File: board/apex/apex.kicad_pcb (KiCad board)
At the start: 2 copper layers, 1 part

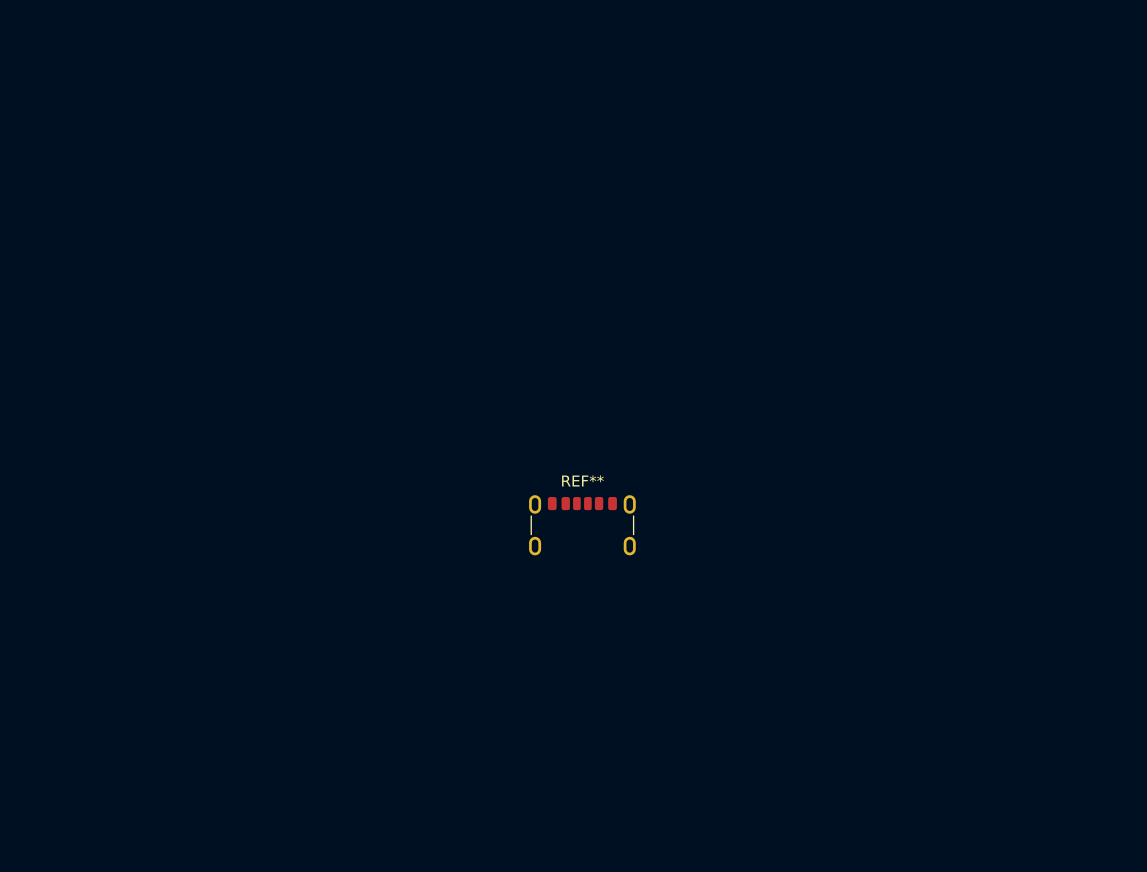
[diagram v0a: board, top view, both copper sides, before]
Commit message: added power input/outputs
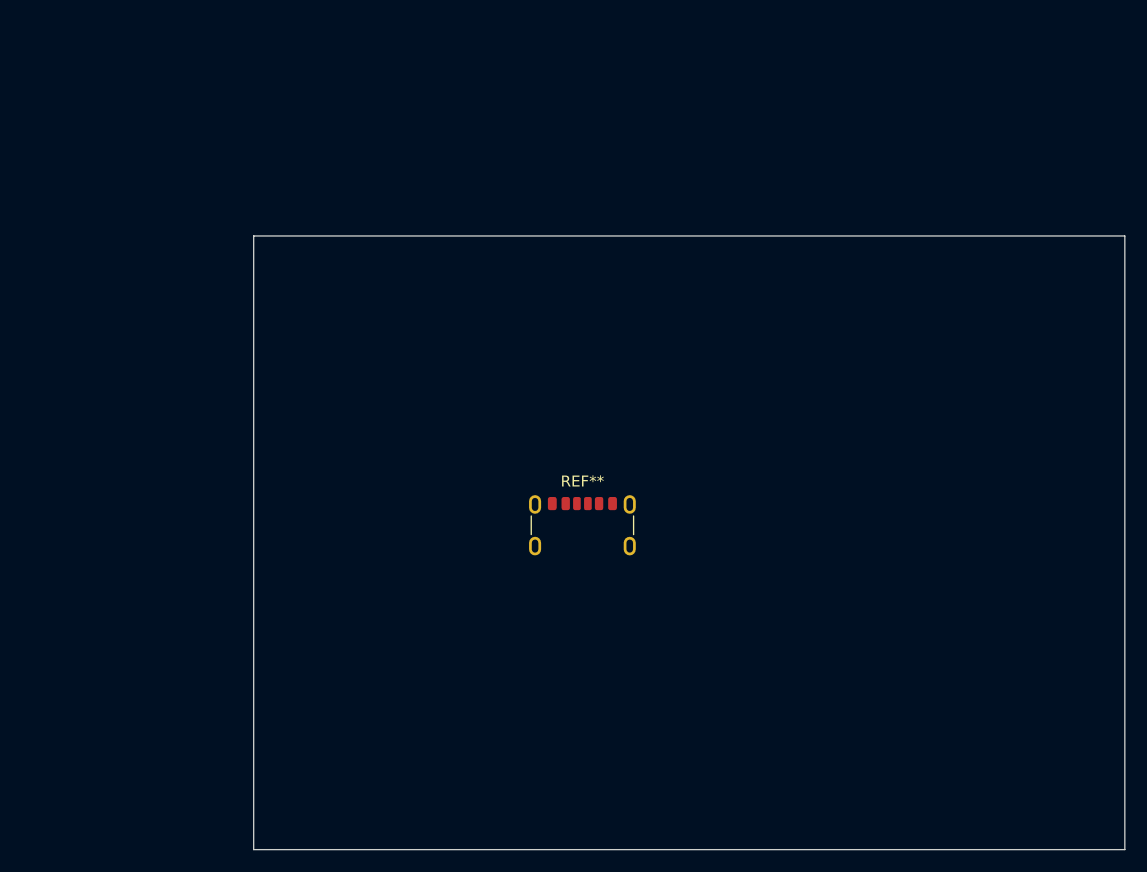
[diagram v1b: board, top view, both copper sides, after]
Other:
- board outline added: 79.5 x 56 mm
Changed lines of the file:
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@@
 		)
 	)
+	(gr_line
+		(start 117 50)
+		(end 117 106)
+		(stroke
+			(width 0.05)
+			(type default)
+		)
+		(layer "Edge.Cuts")
+	)
+	(gr_line
+		(start 37.5 106)
+		(end 37.5 50)
+		(stroke
+			(width 0.05)
+			(type default)
+		)
+		(layer "Edge.Cuts")
+	)
+	(gr_line
+		(start 37.5 50)
+		(end 117 50)
+		(stroke
+			(width 0.05)
+			(type default)
+		)
+		(layer "Edge.Cuts")
+	)
+	(gr_line
+		(start 117 106)
+		(end 37.5 106)
+		(stroke
+			(width 0.05)
+			(type default)
+		)
+		(layer "Edge.Cuts")
+	)
 )

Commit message: added SMDs to board
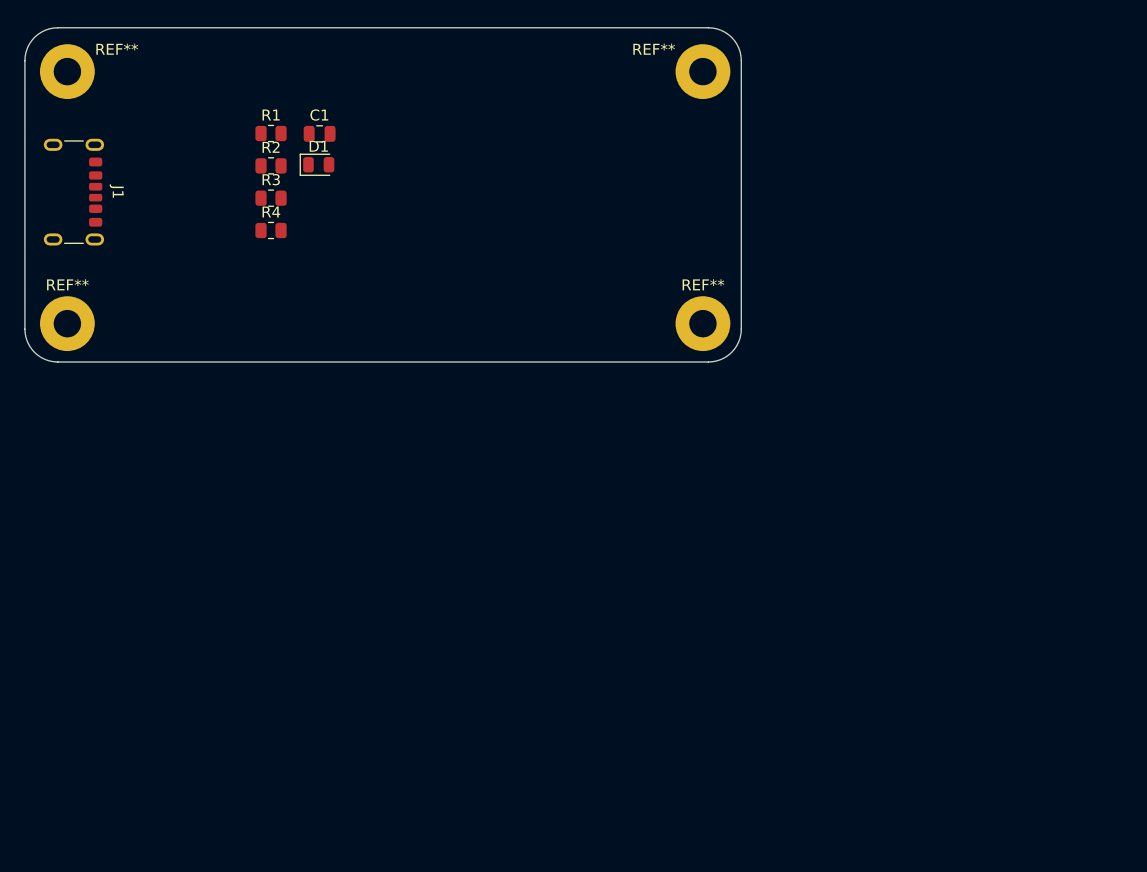
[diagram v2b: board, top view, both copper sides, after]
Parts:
- removed the REF** at (67.5, 77.5)
- added C1: 0.1uF, Capacitor_SMD:C_0805_2012Metric, F.Cu at (43.5, 40.7)
- added D1: LED, LED_SMD:LED_0805_2012Metric, F.Cu at (43.4, 43.5)
- added J1: USB_C_Receptacle_PowerOnly_6P, Connector_USB:USB_C_Receptacle_GCT_USB4125-xx-x-0190_6P_TopMnt_Horizontal, F.Cu at (20.0, 46.0)
- added R1: R, Resistor_SMD:R_0805_2012Metric, F.Cu at (39.1, 40.6)
- added R2: 5.1k, Resistor_SMD:R_0805_2012Metric, F.Cu at (39.1, 43.6)
- added R3: 5.1k, Resistor_SMD:R_0805_2012Metric, F.Cu at (39.1, 46.5)
- added R4: 330, Resistor_SMD:R_0805_2012Metric, F.Cu at (39.1, 49.5)
- added REF**: MountingHole_2.5mm_Pad, MountingHole:MountingHole_2.5mm_Pad, F.Cu at (20.5, 35.0)
- added REF**: MountingHole_2.5mm_Pad, MountingHole:MountingHole_2.5mm_Pad, F.Cu at (20.5, 58.0)
- added REF**: MountingHole_2.5mm_Pad, MountingHole:MountingHole_2.5mm_Pad, F.Cu at (78.5, 35.0)
- added REF**: MountingHole_2.5mm_Pad, MountingHole:MountingHole_2.5mm_Pad, F.Cu at (78.5, 58.0)
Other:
- board size 79.5 x 56 mm -> 65.4 x 30.5 mm

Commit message: started routing
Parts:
- moved R4 10.6 mm to (30.0, 55.0)
- moved R3 9.72 mm to (30.0, 50.0)
- moved R2 9.19 mm to (30.0, 45.0)
- moved R1 9.11 mm to (30.0, 40.0)
- moved D1 8.57 mm to (35.0, 45.0)
- moved C1 8.54 mm to (35.0, 40.0)
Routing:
- net GND: track 0.00 -> 13.9 mm
- net VBUS: track 0.00 -> 9.69 mm
- net Net-(J1-CC1): track 0.00 -> 7.87 mm
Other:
- copper layers 2 -> 4
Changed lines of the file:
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@@
 	(layers
 		(0 "F.Cu" signal)
+		(1 "In1.Cu" signal)
+		(2 "In2.Cu" signal)
 		(31 "B.Cu" signal)
 		(32 "B.Adhes" user "B.Adhesive")
@@
 			)
 			(layer "dielectric 1"
+				(type "prepreg")
+				(thickness 0.1)
+				(material "FR4")
+				(epsilon_r 4.5)
+				(loss_tangent 0.02)
+			)
+			(layer "In1.Cu"
+				(type "copper")
+				(thickness 0.035)
+			)
+			(layer "dielectric 2"
 				(type "core")
-				(thickness 1.51)
+				(thickness 1.24)
+				(material "FR4")
+				(epsilon_r 4.5)
+				(loss_tangent 0.02)
+			)
+			(layer "In2.Cu"
+				(type "copper")
+				(thickness 0.035)
+			)
+			(layer "dielectric 3"
+				(type "prepreg")
+				(thickness 0.1)
 				(material "FR4")
 				(epsilon_r 4.5)
@@
 	(footprint "Resistor_SMD:R_0805_2012Metric"
 		(layer "F.Cu")
-		(at 39.0875 43.6)
+		(at 30 45)
 		(descr "Resistor SMD 0805 (2012 Metric), square (rectangular) end terminal, IPC_7351 nominal, (Body size source: IPC-SM-782 page 72, https://www.pcb-3d.com/wordpress/wp-content/uploads/ipc-sm-782a_amendment_1_and_2.pdf), generated with kicad-footprint-generator")
 		(tags "resistor")
@@
 	(footprint "Resistor_SMD:R_0805_2012Metric"
 		(layer "F.Cu")
-		(at 39.0875 49.5)
+		(at 30 55)
 		(descr "Resistor SMD 0805 (2012 Metric), square (rectangular) end terminal, IPC_7351 nominal, (Body size source: IPC-SM-782 page 72, https://www.pcb-3d.com/wordpress/wp-content/uploads/ipc-sm-782a_amendment_1_and_2.pdf), generated with kicad-footprint-generator")
 		(tags "resistor")
@@
 	(footprint "Capacitor_SMD:C_0805_2012Metric"
 		(layer "F.Cu")
-		(at 43.5175 40.68)
+		(at 35 40)
 		(descr "Capacitor SMD 0805 (2012 Metric), square (rectangular) end terminal, IPC_7351 nominal, (Body size source: IPC-SM-782 page 76, https://www.pcb-3d.com/wordpress/wp-content/uploads/ipc-sm-782a_amendment_1_and_2.pdf, https://docs.google.com/spreadsheets/d/1BsfQQcO9C6DZCsRaXUlFlo91Tg2WpOkGARC1WS5S8t0/edit?usp=sharing), generated with kicad-footprint-generator")
 		(tags "capacitor")
@@
 	(footprint "Resistor_SMD:R_0805_2012Metric"
 		(layer "F.Cu")
-		(at 39.0875 40.65)
+		(at 30 40)
 		(descr "Resistor SMD 0805 (2012 Metric), square (rectangular) end terminal, IPC_7351 nominal, (Body size source: IPC-SM-782 page 72, https://www.pcb-3d.com/wordpress/wp-content/uploads/ipc-sm-782a_amendment_1_and_2.pdf), generated with kicad-footprint-generator")
 		(tags "resistor")
@@
 	(footprint "Resistor_SMD:R_0805_2012Metric"
 		(layer "F.Cu")
-		(at 39.0875 46.55)
+		(at 30 50)
 		(descr "Resistor SMD 0805 (2012 Metric), square (rectangular) end terminal, IPC_7351 nominal, (Body size source: IPC-SM-782 page 72, https://www.pcb-3d.com/wordpress/wp-content/uploads/ipc-sm-782a_amendment_1_and_2.pdf), generated with kicad-footprint-generator")
 		(tags "resistor")
@@
 	(footprint "LED_SMD:LED_0805_2012Metric"
 		(layer "F.Cu")
-		(at 43.4375 43.5)
+		(at 35 45)
 		(descr "LED SMD 0805 (2012 Metric), square (rectangular) end terminal, IPC_7351 nominal, (Body size source: https://docs.google.com/spreadsheets/d/1BsfQQcO9C6DZCsRaXUlFlo91Tg2WpOkGARC1WS5S8t0/edit?usp=sharing), generated with kicad-footprint-generator")
 		(tags "LED")
@@
 			(extension_offset 0) keep_text_aligned)
 	)
+	(segment
+		(start 29.0875 50)
+		(end 24.5875 45.5)
+		(width 0.2)
+		(layer "F.Cu")
+		(net 1)
+	)
+	(segment
+		(start 24.5875 45.5)
+		(end 23.08 45.5)
+		(width 0.2)
+		(layer "F.Cu")
+		(net 1)
+	)
+	(segment
+		(start 34.0625 45)
+		(end 30.9125 45)
+		(width 0.2)
+		(layer "F.Cu")
+		(net 2)
+	)
+	(segment
+		(start 30.9125 45)
+		(end 30.9125 50)
+		(width 0.2)
+		(layer "F.Cu")
+		(net 2)
+	)
+	(segment
+		(start 30.9125 53.175)
+		(end 29.0875 55)
+		(width 0.2)
+		(layer "F.Cu")
+		(net 2)
+	)
+	(segment
+		(start 30.9125 50)
+		(end 30.9125 53.175)
+		(width 0.2)
+		(layer "F.Cu")
+		(net 2)
+	)
+	(segment
+		(start 26.4325 44.48)
+		(end 23.08 44.48)
+		(width 0.2)
+		(layer "F.Cu")
+		(net 3)
+	)
+	(segment
+		(start 30.9125 40)
+		(end 26.4325 44.48)
+		(width 0.2)
+		(layer "F.Cu")
+		(net 3)
+	)
 )

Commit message: organized modules
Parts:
- removed D1: LED, LED_SMD:LED_0805_2012Metric
- added C2: 10 uF, Capacitor_SMD:C_0805_2012Metric, F.Cu at (48.0, 54.0)
- added C3: 10 uF, Capacitor_SMD:C_0805_2012Metric, F.Cu at (57.5, 54.0)
- added LED1: 150080BS75000, LEDBS75000_WRE:LED_BS75000_WRE, F.Cu at (65.5, 54.0)
- added U1: AP7363-33D-13, AP7363_33D_13:TO252-3L_DIO, F.Cu at (52.8, 49.9)
- C1: value 0.1uF -> 0.1 uF
- J1: value USB_C_Receptacle_PowerOnly_6P -> USB4125-GF-A_REVA2; footprint Connector_USB:USB_C_Receptacle_GCT_USB4125-xx-x-0190_6P_TopMnt_Horizontal -> USB4125_GF_A:GCT_USB4125-GF-A_REVA2
- R1: value R -> 3.3
- moved R1 34.5 mm to (61.5, 54.1), turned to -90 degrees
- moved C1 15.2 mm to (39.5, 54.5), turned to -90 degrees
- moved R4 6.52 mm to (36.5, 54.5), turned to -90 degrees
- moved R3 5.55 mm to (27.6, 45.0)
- moved R2 3.13 mm to (27.6, 47.0)
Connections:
- R1 pad 2: VBUS -> +3V3
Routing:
- net (no net): track 0.00 -> 21.2 mm, vias 0 -> 7
- net GND: track 13.9 -> 27.4 mm
- net +3V3: track 0.00 -> 7.05 mm
- net VBUS: track 9.69 -> 3.14 mm
- net Net-(J1-CC1): track 7.87 -> 3.80 mm
- net Net-(LED1-Pad2): track 0.00 -> 4.01 mm
- net Net-(J1-CC2): track 0.00 -> 3.80 mm
- net GNDPWR: track 0.00 -> 3.04 mm

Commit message: checked parity with schematic
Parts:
- H1: renamed from REF**; value MountingHole_2.5mm_Pad -> H1_MH
- H2: renamed from REF**; value MountingHole_2.5mm_Pad -> H2_MH
- H3: renamed from REF**; value MountingHole_2.5mm_Pad -> H3_MH
- H4: renamed from REF**; value MountingHole_2.5mm_Pad -> H4_MH
- moved LED1 15.5 mm to (50.0, 53.1)
- moved C2 14.3 mm to (33.7, 53.1)
- moved C3 14.3 mm to (43.2, 53.1)
- moved R1 14.3 mm to (47.2, 53.1)
- moved U1 14.3 mm to (38.5, 49.0)
- moved C1 11.1 mm to (28.5, 53.0)
- moved R4 11.1 mm to (25.5, 52.9)
- moved J1 0.50 mm to (20.5, 46.0)
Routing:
- net GND: track 27.4 -> 50.2 mm, vias 0 -> 2
- net (no net): track 21.2 -> 0.00 mm, vias 7 -> 0
- net VBUS: track 3.14 -> 23.1 mm, vias 0 -> 3
- net Net-(LED1-Pad2): track 4.01 -> 2.80 mm
- net Net-(J1-CC2): track 3.80 -> 3.30 mm
- net Net-(J1-CC1): track 3.80 -> 3.30 mm
